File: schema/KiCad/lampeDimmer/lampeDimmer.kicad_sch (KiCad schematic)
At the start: 17 parts, among them J1 PICkit4, J2 USART, J3 EXT_IO, J4 EXT_PWM4B, J5 EXT_PWM4D, J6 EXT_ADC1, J7 CON_POT_SW, J8 Entrée, J9 Sortie, M1 ARDUINO_MICRO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

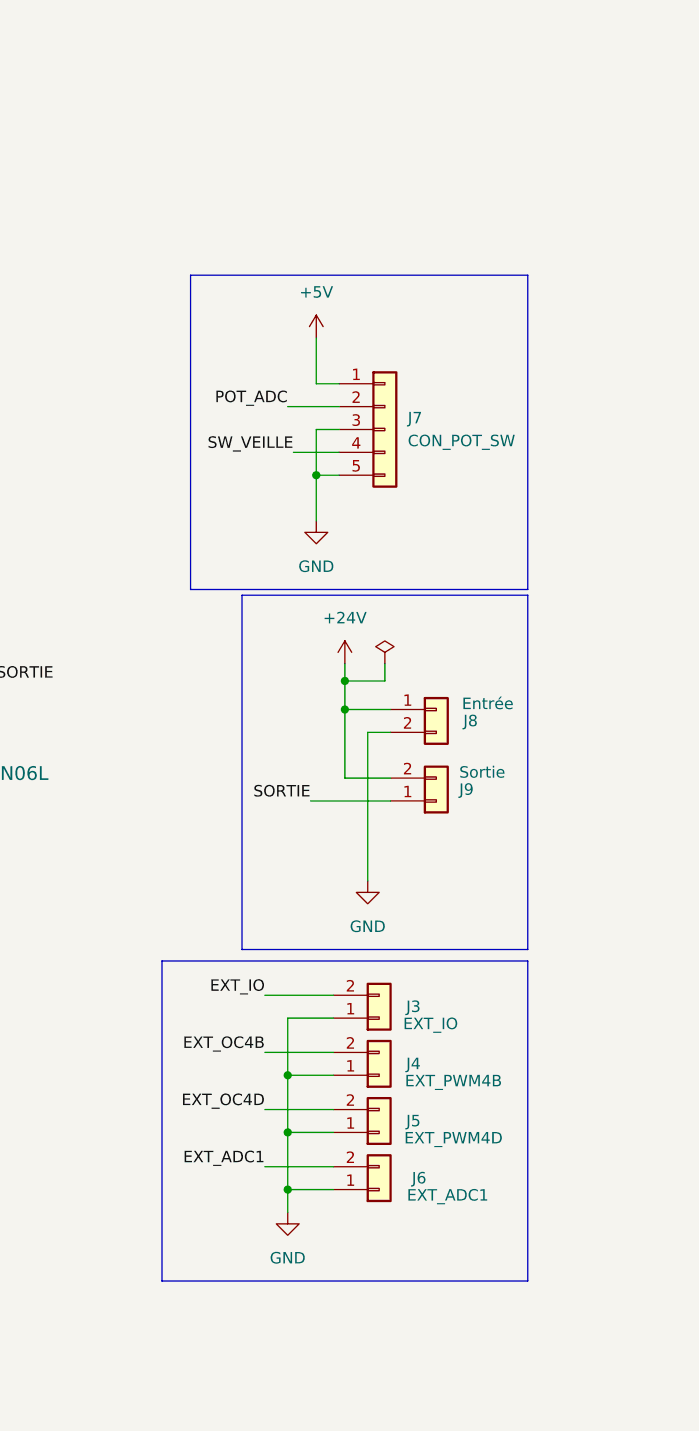
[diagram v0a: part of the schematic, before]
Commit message: [SCHÉMA + PCB]
+ Ajout de test point;
~ Traces et dégagements augmentés;
~ Rapprochement des condensateurs de découplage des composants;

+ Fichiers Gerber générés.
~ Grosseur du text augmenté.
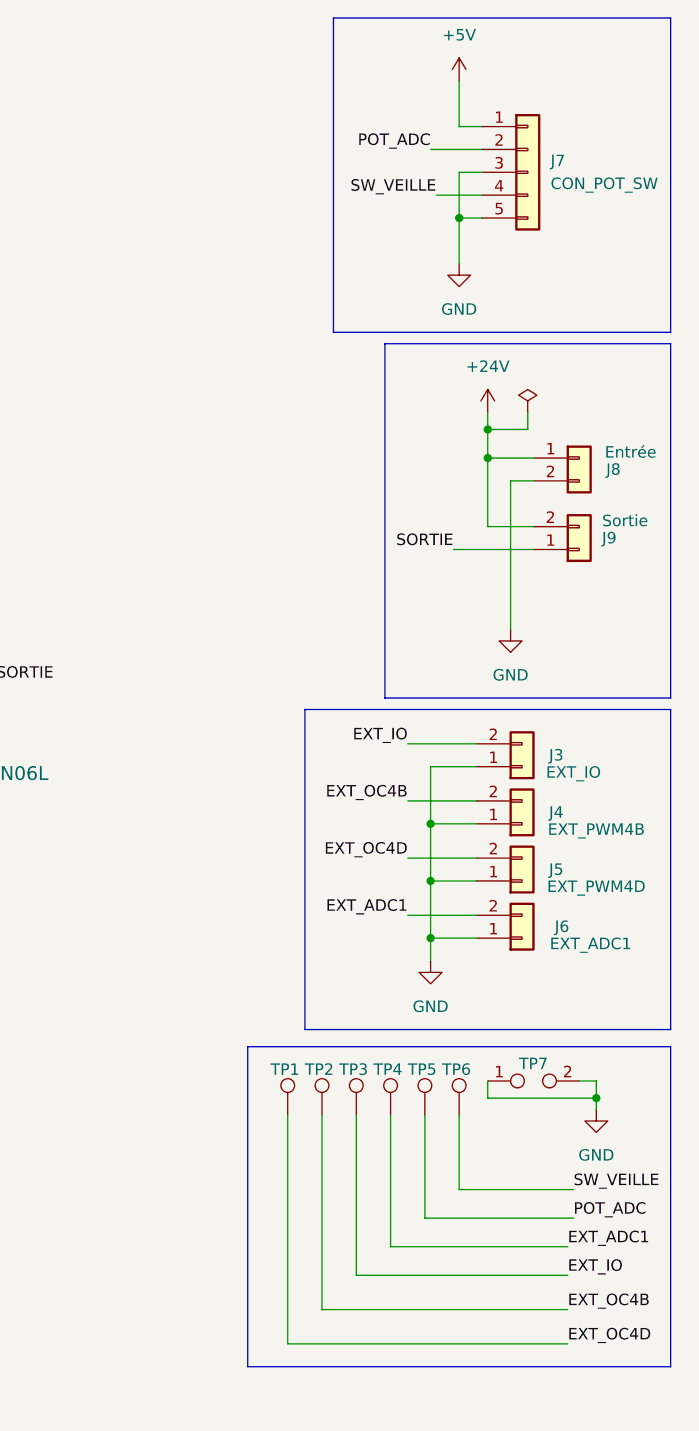
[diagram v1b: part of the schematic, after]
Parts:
- added TP1, TP2, TP3, TP4, TP5, TP6: TestPoint, THOMAS_library:TestPoint_Keystone_5000-5004_Miniature-Resistor, symbol Connector:TestPoint
- added TP7: TestPoint_2Pole, THOMAS_library:TestPoint_Bridge_Pitch7.08mm_Drill2.0mm, symbol Connector:TestPoint_2Pole
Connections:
- net EXT_ADC1: now also TP4.1
- net EXT_IO: now also TP3.1
- net EXT_OC4B: now also TP2.1
- net EXT_OC4D: now also TP1.1
- net GND: now also TP7.1, TP7.2
- net POT_ADC: now also TP5.1
- net SW_VEILLE: now also TP6.1
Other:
- moved on the sheet: J3, J4, J5, J6, J7, J8, J9

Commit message: ~ Correction des erreurs de la précédente version du PCB:   - Trace sur le mauvais côté.   - Élargissement des traces.
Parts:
- C1, C2, C3: footprint Capacitor_THT:C_Disc_D6.0mm_W2.5mm_P5.00mm -> Capacitor_THT:C_Disc_D3.0mm_W2.0mm_P2.50mm
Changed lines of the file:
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@@
     (property "Reference" "C3" (id 0) (at 142.875 39.37 90))
     (property "Value" "100nF" (id 1) (at 142.875 41.91 90))
-    (property "Footprint" "Capacitor_THT:C_Disc_D6.0mm_W2.5mm_P5.00mm" (id 2) (at 146.685 46.0248 0)
+    (property "Footprint" "Capacitor_THT:C_Disc_D3.0mm_W2.0mm_P2.50mm" (id 2) (at 146.685 46.0248 0)
       (effects (font (size 1.27 1.27)) hide)
     )
@@
     (property "Reference" "C2" (id 0) (at 107.95 155.575 90))
     (property "Value" "100nF" (id 1) (at 107.95 158.115 90))
-    (property "Footprint" "Capacitor_THT:C_Disc_D6.0mm_W2.5mm_P5.00mm" (id 2) (at 111.76 150.7998 0)
+    (property "Footprint" "Capacitor_THT:C_Disc_D3.0mm_W2.0mm_P2.50mm" (id 2) (at 111.76 150.7998 0)
       (effects (font (size 1.27 1.27)) hide)
     )
@@
     (property "Reference" "C1" (id 0) (at 86.995 44.45 90))
     (property "Value" "100nF" (id 1) (at 86.995 46.99 90))
-    (property "Footprint" "Capacitor_THT:C_Disc_D6.0mm_W2.5mm_P5.00mm" (id 2) (at 90.805 51.1048 0)
+    (property "Footprint" "Capacitor_THT:C_Disc_D3.0mm_W2.0mm_P2.50mm" (id 2) (at 90.805 51.1048 0)
       (effects (font (size 1.27 1.27)) hide)
     )
@@
     )
     (path "/731ace02-ca5b-4098-acb6-9d833fcdd311"
-      (reference "C1") (unit 1) (value "100nF") (footprint "Capacitor_THT:C_Disc_D6.0mm_W2.5mm_P5.00mm")
+      (reference "C1") (unit 1) (value "100nF") (footprint "Capacitor_THT:C_Disc_D3.0mm_W2.0mm_P2.50mm")
     )
     (path "/31fe16cb-cf2e-4116-a618-5a413e6b65d6"
-      (reference "C2") (unit 1) (value "100nF") (footprint "Capacitor_THT:C_Disc_D6.0mm_W2.5mm_P5.00mm")
+      (reference "C2") (unit 1) (value "100nF") (footprint "Capacitor_THT:C_Disc_D3.0mm_W2.0mm_P2.50mm")
     )
     (path "/2431b9c8-7adb-413e-80ec-3d8d3c0a0a6c"
-      (reference "C3") (unit 1) (value "100nF") (footprint "Capacitor_THT:C_Disc_D6.0mm_W2.5mm_P5.00mm")
+      (reference "C3") (unit 1) (value "100nF") (footprint "Capacitor_THT:C_Disc_D3.0mm_W2.0mm_P2.50mm")
     )
     (path "/0ab0a148-2e00-4d0f-99f7-41cfe765f1a4"
